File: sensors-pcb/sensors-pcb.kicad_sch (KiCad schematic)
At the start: 15 parts, among them U1 MAX-M8Q

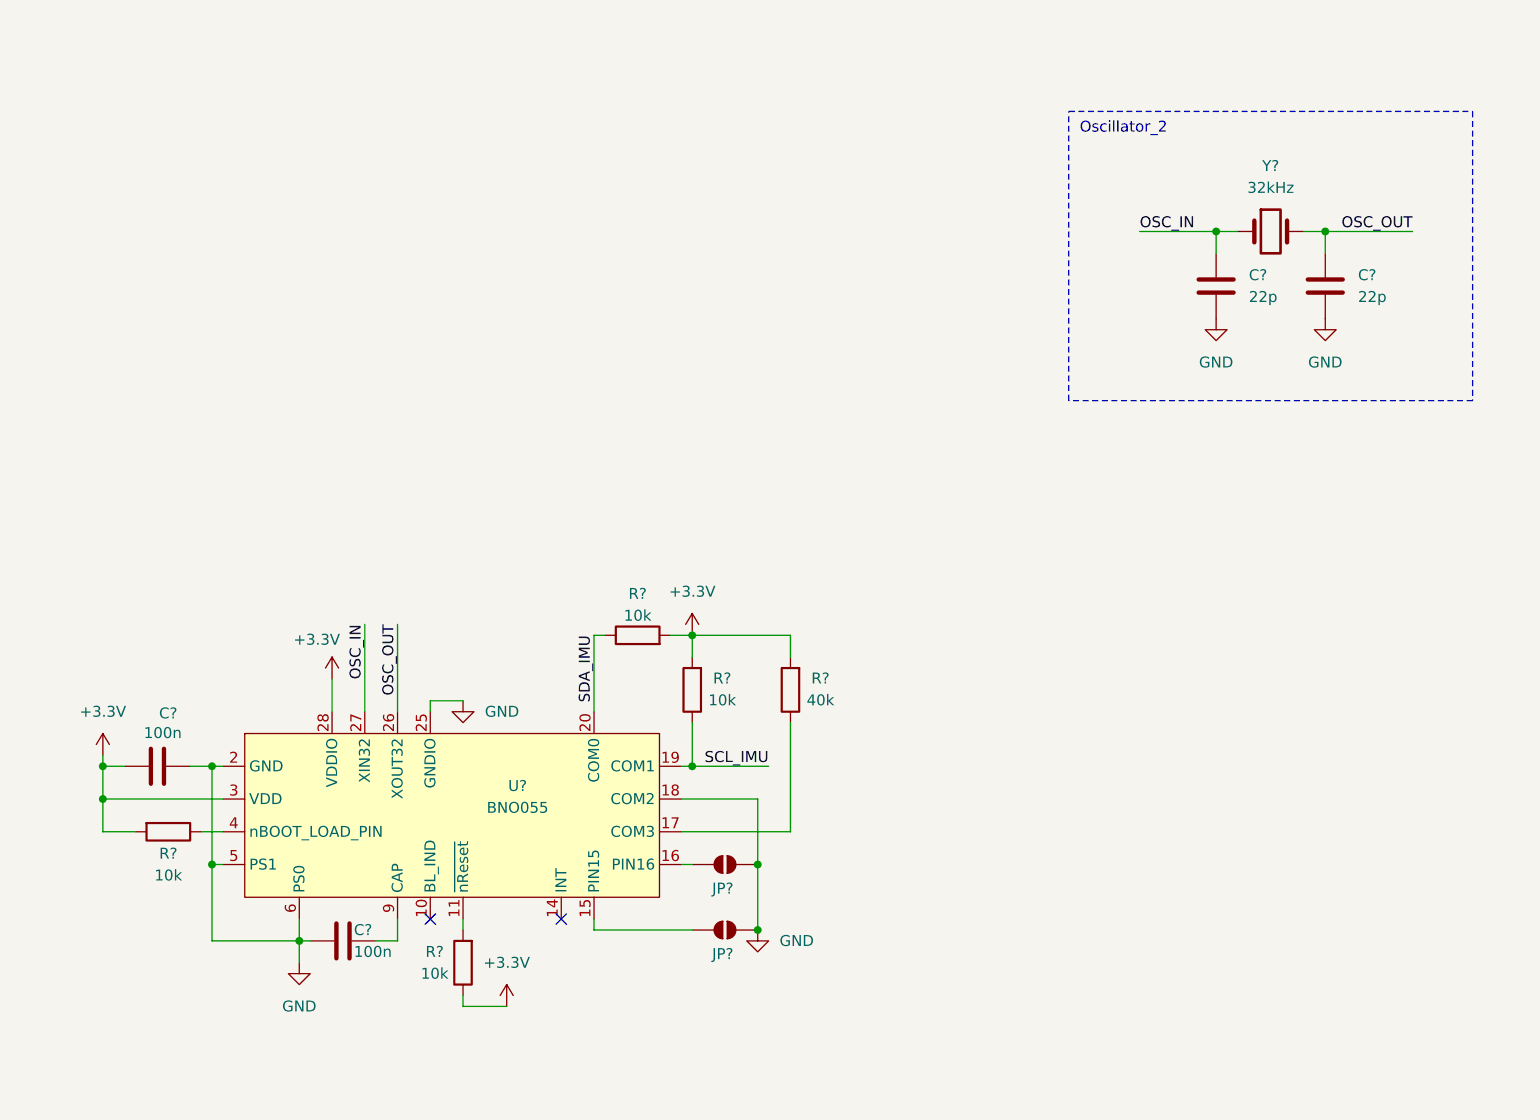
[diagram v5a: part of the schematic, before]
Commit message: sensors-pcb: add footprints
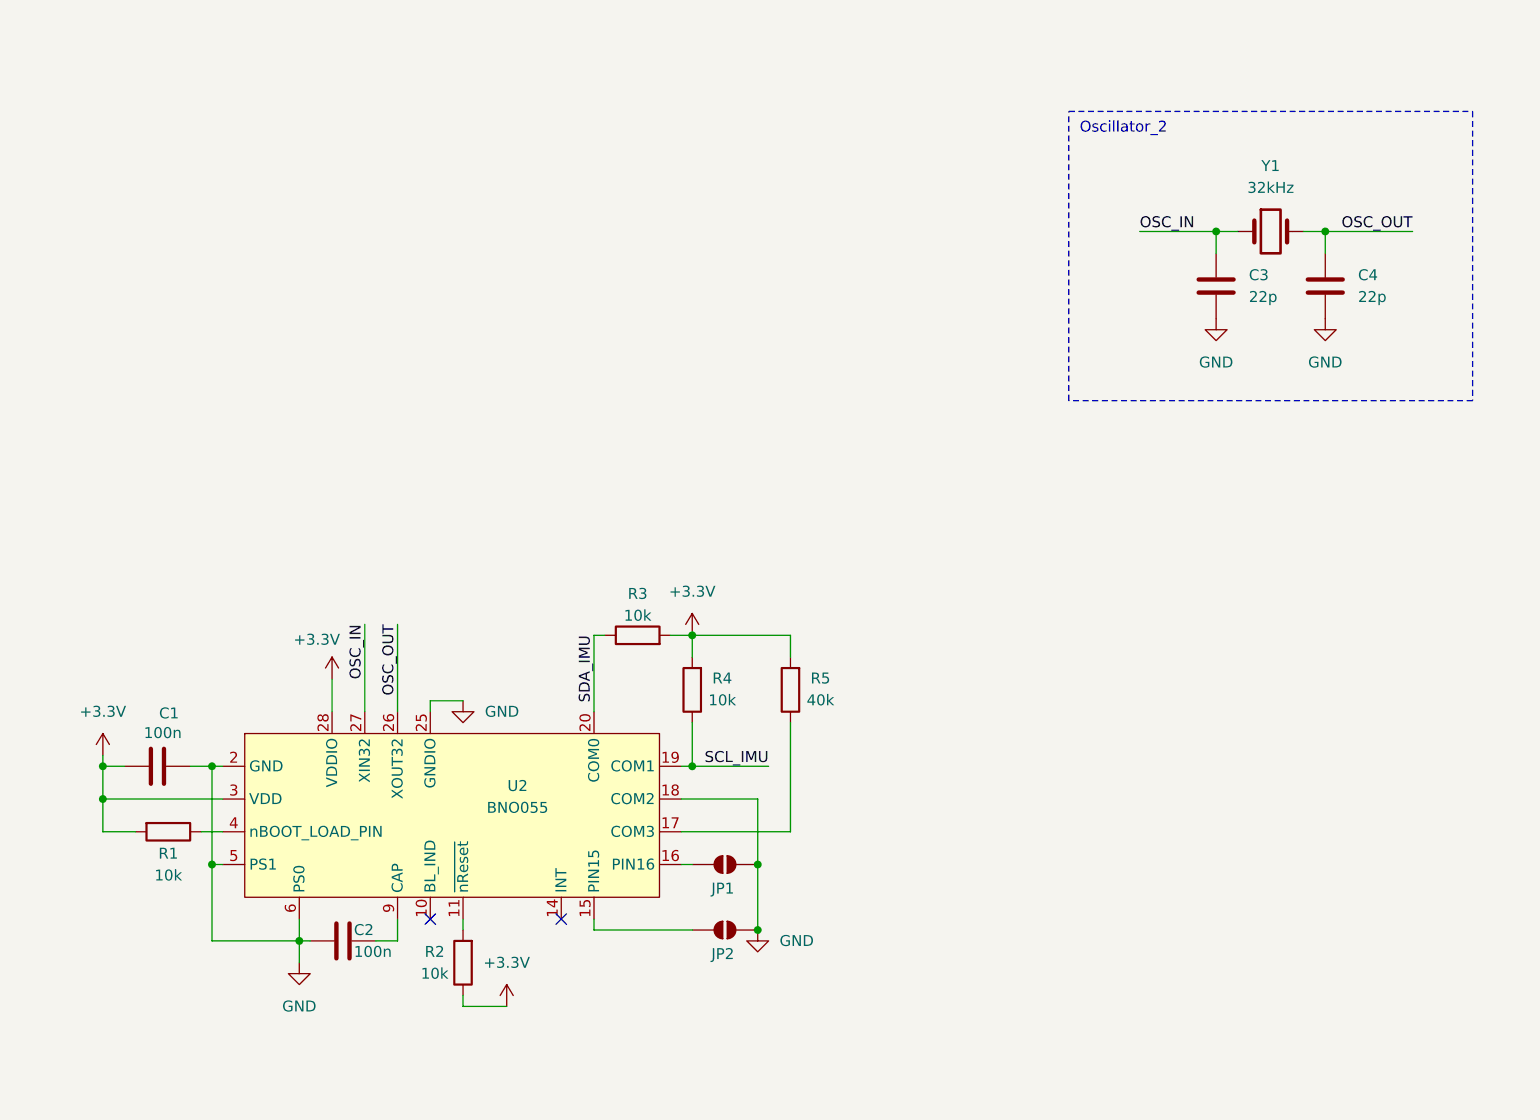
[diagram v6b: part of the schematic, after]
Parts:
- C1, C2: renamed from C?; footprint (none) -> Capacitor_SMD:C_0603_1608Metric
- JP1, JP2: renamed from JP?; footprint (none) -> Jumper:SolderJumper-2_P1.3mm_Bridged_RoundedPad1.0x1.5mm
- R1, R2, R3, R4, R5: renamed from R?; footprint (none) -> Resistor_SMD:R_0402_1005Metric
- U2: renamed from U?; footprint (none) -> Package_LGA:LGA-28_5.2x3.8mm_P0.5mm
- gave numbers to parts that had none: 3
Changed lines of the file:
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@@
 		(dnp no)
 		(fields_autoplaced yes)
-		(property "Reference" "Y?"
+		(property "Reference" "Y1"
 			(at 260.35 19.05 0)
 			(effects
@@
 			(project "sensors-pcb"
 				(path "/4b4cf3aa-c94c-4150-b9c5-35049cd71136"
-					(reference "Y?")
+					(reference "Y1")
 					(unit 1)
 				)
@@
 		(on_board yes)
 		(dnp no)
-		(property "Reference" "C?"
+		(property "Reference" "C2"
 			(at 153.67 107.95 90)
 			(effects
@@
 			)
 		)
-		(property "Footprint" ""
+		(property "Footprint" "Capacitor_SMD:C_0603_1608Metric"
 			(at 148.59 110.1852 0)
 			(effects
@@
 			(project ""
 				(path "/4b4cf3aa-c94c-4150-b9c5-35049cd71136"
-					(reference "C?")
+					(reference "C2")
 					(unit 1)
 				)
@@
 		(on_board yes)
 		(dnp no)
-		(property "Reference" "JP?"
+		(property "Reference" "JP1"
 			(at 196.596 103.124 0)
 			(effects
@@
 			)
 		)
-		(property "Footprint" ""
+		(property "Footprint" "Jumper:SolderJumper-2_P1.3mm_Bridged_RoundedPad1.0x1.5mm"
 			(at 196.85 100.33 0)
 			(effects
@@
 			(project "sensors-pcb"
 				(path "/4b4cf3aa-c94c-4150-b9c5-35049cd71136"
-					(reference "JP?")
+					(reference "JP1")
 					(unit 1)
 				)
@@
 		(dnp no)
 		(fields_autoplaced yes)
-		(property "Reference" "#PWR?"
+		(property "Reference" "#PWR0106"
 			(at 200.66 114.3 0)
 			(effects
@@
 			(project "sensors-pcb"
 				(path "/4b4cf3aa-c94c-4150-b9c5-35049cd71136"
-					(reference "#PWR?")
+					(reference "#PWR0106")
 					(unit 1)
 				)
@@
 		(dnp no)
 		(fields_autoplaced yes)
-		(property "Reference" "#PWR?"
+		(property "Reference" "#PWR0101"
 			(at 193.04 77.47 0)
 			(effects
@@
 			(project ""
 				(path "/4b4cf3aa-c94c-4150-b9c5-35049cd71136"
-					(reference "#PWR?")
+					(reference "#PWR0101")
 					(unit 1)
 				)
@@
 		(on_board yes)
 		(dnp no)
-		(property "Reference" "U?"
+		(property "Reference" "U2"
 			(at 172.72 91.186 0)
 			(effects
@@
 			)
 		)
-		(property "Footprint" ""
+		(property "Footprint" "Package_LGA:LGA-28_5.2x3.8mm_P0.5mm"
 			(at 148.59 96.52 0)
 			(effects
@@
 			(project ""
 				(path "/4b4cf3aa-c94c-4150-b9c5-35049cd71136"
-					(reference "U?")
+					(reference "U2")
 					(unit 1)
 				)
@@
 		(on_board yes)
 		(dnp no)
-		(property "Reference" "#PWR?"
+		(property "Reference" "#PWR0108"
 			(at 151.13 82.55 0)
 			(effects
@@
 			(project "sensors-pcb"
 				(path "/4b4cf3aa-c94c-4150-b9c5-35049cd71136"
-					(reference "#PWR?")
+					(reference "#PWR0108")
 					(unit 1)
 				)
@@
 		(dnp no)
 		(fields_autoplaced yes)
-		(property "Reference" "C?"
+		(property "Reference" "C3"
 			(at 257.81 31.7499 0)
 			(effects
@@
 			(project "sensors-pcb"
 				(path "/4b4cf3aa-c94c-4150-b9c5-35049cd71136"
-					(reference "C?")
+					(reference "C3")
 					(unit 1)
 				)
@@
 		(on_board yes)
 		(dnp no)
-		(property "Reference" "JP?"
+		(property "Reference" "JP2"
 			(at 196.596 110.744 0)
 			(effects
@@
 			)
 		)
-		(property "Footprint" ""
+		(property "Footprint" "Jumper:SolderJumper-2_P1.3mm_Bridged_RoundedPad1.0x1.5mm"
 			(at 196.85 107.95 0)
 			(effects
@@
 			(project ""
 				(path "/4b4cf3aa-c94c-4150-b9c5-35049cd71136"
-					(reference "JP?")
+					(reference "JP2")
 					(unit 1)
 				)
@@
 		(on_board yes)
 		(dnp no)
-		(property "Reference" "R?"
+		(property "Reference" "R2"
 			(at 163.068 110.49 0)
 			(effects
@@
 			)
 		)
-		(property "Footprint" ""
+		(property "Footprint" "Resistor_SMD:R_0402_1005Metric"
 			(at 168.148 111.76 90)
 			(effects
@@
 			(project "sensors-pcb"
 				(path "/4b4cf3aa-c94c-4150-b9c5-35049cd71136"
-					(reference "R?")
+					(reference "R2")
 					(unit 1)
 				)
@@
 		(dnp no)
 		(fields_autoplaced yes)
-		(property "Reference" "#PWR?"
+		(property "Reference" "#PWR0104"
 			(at 147.32 118.11 0)
 			(effects
@@
 			(project "sensors-pcb"
 				(path "/4b4cf3aa-c94c-4150-b9c5-35049cd71136"
-					(reference "#PWR?")
+					(reference "#PWR0104")
 					(unit 1)
 				)
@@
 		(on_board yes)
 		(dnp no)
-		(property "Reference" "C?"
+		(property "Reference" "C1"
 			(at 131.0005 82.7405 90)
 			(effects
@@
 			)
 		)
-		(property "Footprint" ""
+		(property "Footprint" "Capacitor_SMD:C_0603_1608Metric"
 			(at 134.62 87.9348 0)
 			(effects
@@
 			(project ""
 				(path "/4b4cf3aa-c94c-4150-b9c5-35049cd71136"
-					(reference "C?")
+					(reference "C1")
 					(unit 1)
 				)
@@
 		(dnp no)
 		(fields_autoplaced yes)
-		(property "Reference" "#PWR?"
+		(property "Reference" "#PWR0107"
 			(at 171.45 120.65 0)
 			(effects
@@
 			(project ""
 				(path "/4b4cf3aa-c94c-4150-b9c5-35049cd71136"
-					(reference "#PWR?")
+					(reference "#PWR0107")
 					(unit 1)
 				)
@@
 		(dnp no)
 		(fields_autoplaced yes)
-		(property "Reference" "#PWR?"
+		(property "Reference" "#PWR0109"
 			(at 166.37 87.63 0)
 			(effects
@@
 			(project ""
 				(path "/4b4cf3aa-c94c-4150-b9c5-35049cd71136"
-					(reference "#PWR?")
+					(reference "#PWR0109")
 					(unit 1)
 				)
@@
 		(dnp no)
 		(fields_autoplaced yes)
-		(property "Reference" "#PWR?"
+		(property "Reference" "#PWR0102"
 			(at 254 43.18 0)
 			(effects
@@
 			(project "sensors-pcb"
 				(path "/4b4cf3aa-c94c-4150-b9c5-35049cd71136"
-					(reference "#PWR?")
+					(reference "#PWR0102")
 					(unit 1)
 				)
@@
 		(on_board yes)
 		(dnp no)
-		(property "Reference" "R?"
+		(property "Reference" "R5"
 			(at 207.9625 78.6765 0)
 			(effects
@@
 			)
 		)
-		(property "Footprint" ""
+		(property "Footprint" "Resistor_SMD:R_0402_1005Metric"
 			(at 206.248 80.01 90)
 			(effects
@@
 			(project "sensors-pcb"
 				(path "/4b4cf3aa-c94c-4150-b9c5-35049cd71136"
-					(reference "R?")
+					(reference "R5")
 					(unit 1)
 				)
@@
 		(on_board yes)
 		(dnp no)
-		(property "Reference" "R?"
+		(property "Reference" "R4"
 			(at 196.5325 78.6765 0)
 			(effects
@@
 			)
 		)
-		(property "Footprint" ""
+		(property "Footprint" "Resistor_SMD:R_0402_1005Metric"
 			(at 194.818 80.01 90)
 			(effects
@@
 			(project "sensors-pcb"
 				(path "/4b4cf3aa-c94c-4150-b9c5-35049cd71136"
-					(reference "R?")
+					(reference "R4")
 					(unit 1)
 				)
@@
 		(dnp no)
 		(fields_autoplaced yes)
-		(property "Reference" "#PWR?"
+		(property "Reference" "#PWR0103"
 			(at 266.7 43.18 0)
 			(effects
@@
 			(project "sensors-pcb"
 				(path "/4b4cf3aa-c94c-4150-b9c5-35049cd71136"
-					(reference "#PWR?")
+					(reference "#PWR0103")
 					(unit 1)
 				)
@@
 		(dnp no)
 		(fields_autoplaced yes)
-		(property "Reference" "#PWR?"
+		(property "Reference" "#PWR0105"
 			(at 124.46 91.44 0)
 			(effects
@@
 			(project "sensors-pcb"
 				(path "/4b4cf3aa-c94c-4150-b9c5-35049cd71136"
-					(reference "#PWR?")
+					(reference "#PWR0105")
 					(unit 1)
 				)
@@
 		(on_board yes)
 		(dnp no)
-		(property "Reference" "R?"
+		(property "Reference" "R3"
 			(at 186.69 68.834 90)
 			(effects
@@
 			)
 		)
-		(property "Footprint" ""
+		(property "Footprint" "Resistor_SMD:R_0402_1005Metric"
 			(at 186.69 75.438 90)
 			(effects
@@
 			(project "sensors-pcb"
 				(path "/4b4cf3aa-c94c-4150-b9c5-35049cd71136"
-					(reference "R?")
+					(reference "R3")
 					(unit 1)
 				)
@@
 		(dnp no)
 		(fields_autoplaced yes)
-		(property "Reference" "C?"
+		(property "Reference" "C4"
 			(at 270.51 31.7499 0)
 			(effects
@@
 			(project "sensors-pcb"
 				(path "/4b4cf3aa-c94c-4150-b9c5-35049cd71136"
-					(reference "C?")
+					(reference "C4")
 					(unit 1)
 				)
@@
 		(on_board yes)
 		(dnp no)
-		(property "Reference" "R?"
+		(property "Reference" "R1"
 			(at 132.08 99.06 90)
 			(effects
@@
 			)
 		)
-		(property "Footprint" ""
+		(property "Footprint" "Resistor_SMD:R_0402_1005Metric"
 			(at 132.08 94.742 90)
 			(effects
@@
 			(project ""
 				(path "/4b4cf3aa-c94c-4150-b9c5-35049cd71136"
-					(reference "R?")
-					(unit 1)
-				)
+					(reference "R1")
+					(unit 1)
+				)

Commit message: sensors-pcb: clean up and fix schematic
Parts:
- Y1: JLCPCB C12674 -> C2237; Part Name X49SM8MSD2SC -> X49SM3579545MSD2SC-1
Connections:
- net I2C3_SCL renamed SCL_GPS
- net I2C3_SDA renamed SDA_GPS
- no-connect marks 2 -> 10
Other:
- sheet STM32 Base Layout ports: added I2C3_SCL, I2C3_SDA; removed none

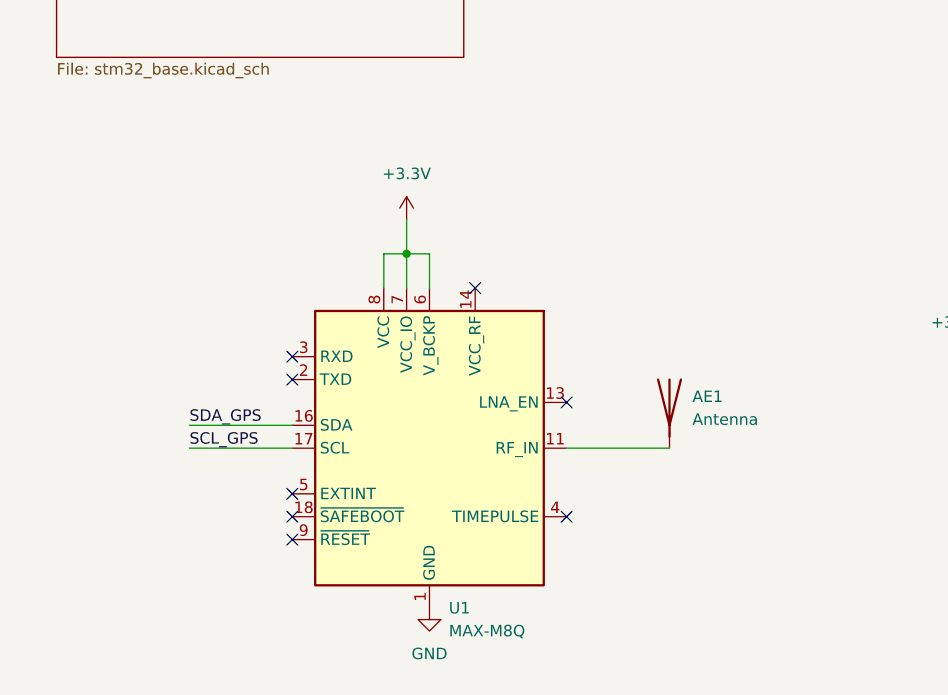
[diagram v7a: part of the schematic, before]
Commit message: sensors-pcb: add coax connector, link JLCPCB numbers
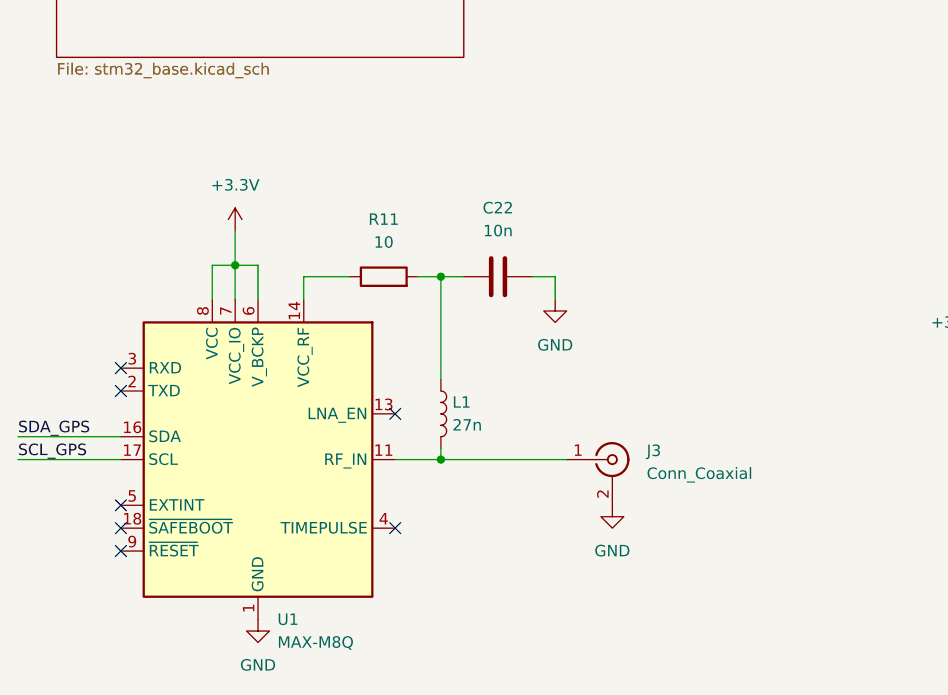
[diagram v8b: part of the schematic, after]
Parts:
- removed AE1: Antenna, symbol Device:Antenna
- added C22: 10n, Capacitor_SMD:C_0402_1005Metric, symbol Device:C
- added J3: Conn_Coaxial, Connector_Coaxial:U.FL_Molex_MCRF_73412-0110_Vertical, symbol Connector:Conn_Coaxial
- added L1: 27n, Inductor_SMD:L_0402_1005Metric, symbol Device:L
- added R11: 10, Resistor_SMD:R_0402_1005Metric, symbol Device:R
- C1, C2: footprint Capacitor_SMD:C_0603_1608Metric -> Capacitor_SMD:C_0402_1005Metric; JLCPCB (none) -> C1525
- R1, R2, R3, R4: JLCPCB (none) -> C25744
- R5: JLCPCB (none) -> C25893
- U1: JLCPCB (none) -> C6898733
- U2: JLCPCB (none) -> C93216
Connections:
- net GND: now also C22.2, J3.2 (Ext)
- net at U1.11 (RF_IN): now also J3.1 (In), L1.2
- net at U1.14 (VCC_RF): now also R11.1
- new net: C22.1, L1.1, R11.2
- no-connect marks 10 -> 9
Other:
- moved on the sheet: U1
